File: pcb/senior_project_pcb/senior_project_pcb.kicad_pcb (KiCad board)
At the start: 4 copper layers, 45 x 45 mm, 55 parts, among them IC1 MAX30102, IC2 ZTP-148SRC1, J1 Conn_01x06, J2 USB_B_Micro, Q1 Q_DUAL_NMOS, Q2 Q_DUAL_NMOS_S1G1D2S2G2D1, SW1 SW_Push_Dual, SW2 SW_Push_Dual, U1 stm32wb55ccu6, U2 MIC5504-1.8YM5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

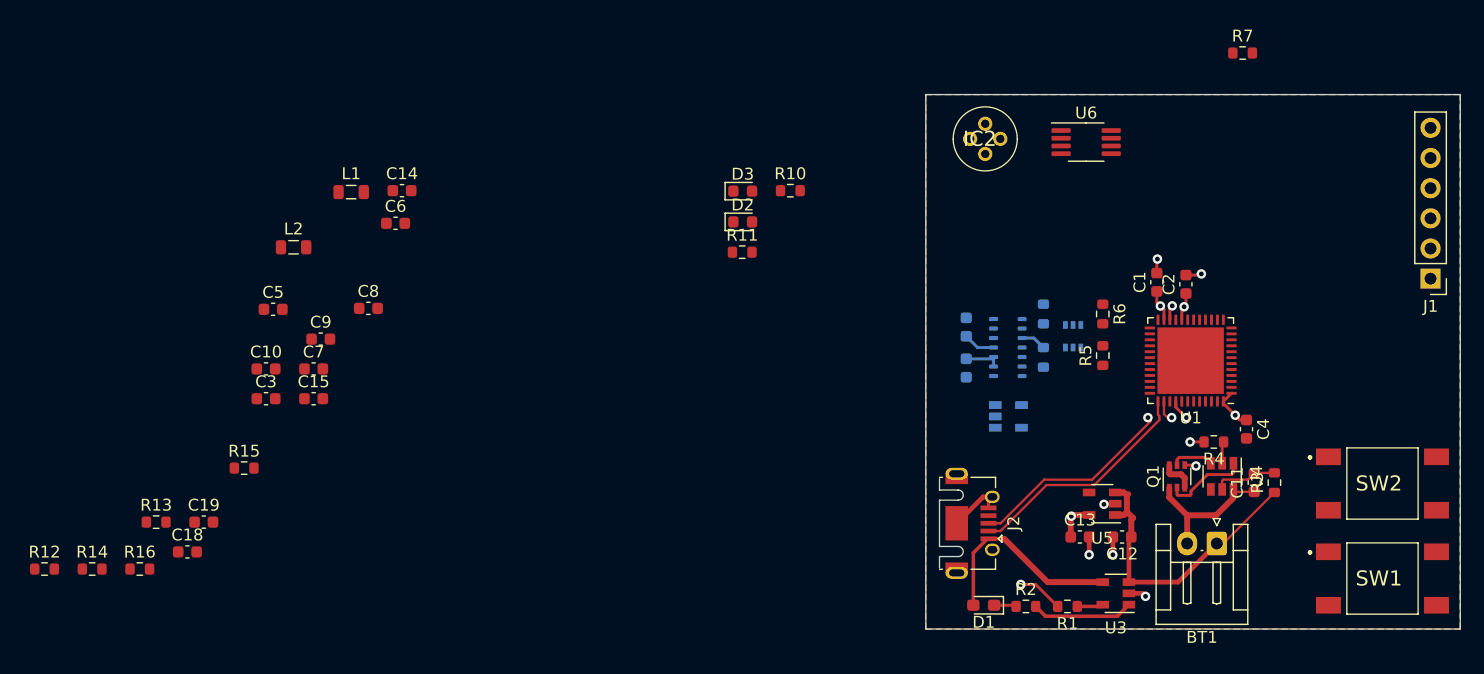
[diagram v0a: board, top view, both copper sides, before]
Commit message: Initial layout mostly done
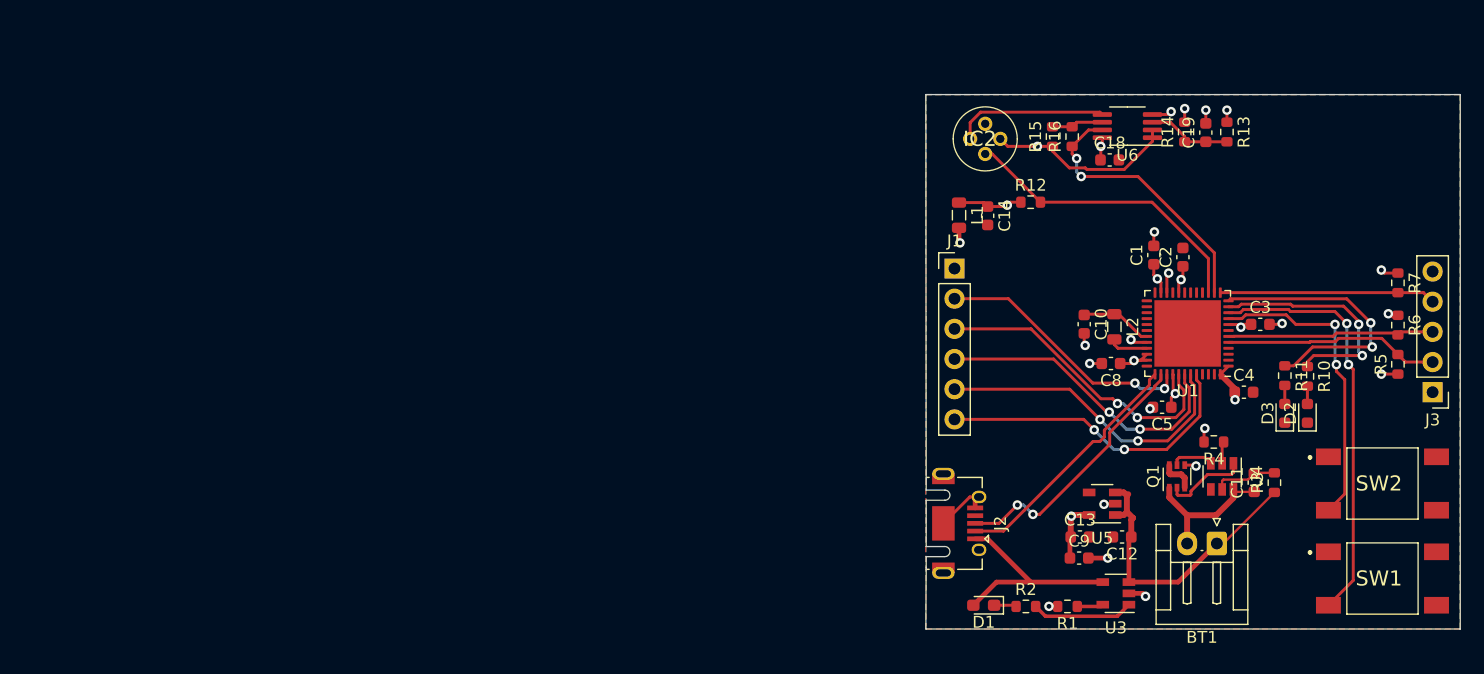
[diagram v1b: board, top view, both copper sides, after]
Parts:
- removed C15: 1u, Capacitor_SMD:C_0603_1608Metric
- removed C16, C17, C6, C7: 100n, Capacitor_SMD:C_0603_1608Metric
- removed IC1: MAX30102, OptoDevice:Maxim_OLGA-14_3.3x5.6mm_P0.8mm
- removed Q2: Q_DUAL_NMOS_S1G1D2S2G2D1, Package_TO_SOT_SMD:SOT-363_SC-70-6
- removed R8, R9: 1k, Resistor_SMD:R_0603_1608Metric
- removed U2: MIC5504-1.8YM5, Package_TO_SOT_SMD:SOT-23-5
- added J3: Conn_01x05, Connector_PinHeader_2.54mm:PinHeader_1x05_P2.54mm_Vertical, F.Cu at (182.7, 75.1)
- C14: value 1u -> 100n
- R5, R6: value 1k -> 2k
- R7: value 10k -> 2k
- moved R14 99.1 mm to (161.8, 53.1), turned to 90 degrees
- moved R13 96.0 mm to (165.4, 53.1), turned to 270 degrees
- moved C19 90.5 mm to (163.6, 53.2), turned to 90 degrees
- moved R12 88.6 mm to (148.8, 59.1)
- moved R16 86.5 mm to (152.3, 53.5), turned to 90 degrees
- moved C18 84.4 mm to (155.5, 55.5)
- moved C3 84.0 mm to (168.2, 69.3)
- moved C5 75.3 mm to (159.9, 76.3), turned to 180 degrees
- moved R15 73.6 mm to (150.7, 53.5), turned to 90 degrees
- moved L2 69.4 mm to (155.9, 69.6), turned to 270 degrees
- moved C10 69.0 mm to (153.3, 69.3), turned to 270 degrees
- moved C9 66.5 mm to (152.9, 89.0)
- moved C8 62.7 mm to (155.6, 72.6), turned to 180 degrees
- moved L1 51.2 mm to (142.8, 60.2), turned to 270 degrees
- moved D2 50.2 mm to (172.1, 76.8), turned to 90 degrees
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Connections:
- C14 pad 1: +3V3 -> +3.3VA
- J1 pad 2: /io/JTAG_TCK -> /io/JTAG_TMS
- J1 pad 3: /io/JTAG_TDI -> /io/JTAG_TCK
- J1 pad 4: /io/JTAG_TDO -> /io/JTAG_TDI
- J1 pad 5: /io/JTAG_TMS -> /io/JTAG_TDO
- R7 pad 2: /Pulse Oximeter/INT -> /INT
- U1 pad 10: /io/LED2 -> /io/BTN1
- U1 pad 11: /io/BTN1 -> /io/LED1
- U1 pad 12: /io/BTN2 -> /io/LED2
- U1 pad 13: Net-(U1-Pad13) -> /INT
- U1 pad 14: Net-(U1-Pad14) -> /thermopile
- U1 pad 15: Net-(U1-Pad15) -> /thermistor
- U1 pad 45: /thermistor -> Net-(U1-Pad45)
- U1 pad 46: /thermopile -> Net-(U1-Pad46)
- U1 pad 9: /io/LED1 -> /io/BTN2
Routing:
- net /io/BTN1: track 0.00 -> 35.4 mm, vias 0 -> 2
- net /io/JTAG_NTRST: track 0.00 -> 26.5 mm, vias 0 -> 2
- net /io/JTAG_TDO: track 0.00 -> 26.4 mm, vias 0 -> 2
- net /io/JTAG_TDI: track 0.00 -> 26.1 mm, vias 0 -> 2
- net /io/BTN2: track 0.00 -> 26.0 mm, vias 0 -> 2
- net /io/JTAG_TCK: track 0.00 -> 25.8 mm, vias 0 -> 2
- net /thermistor: track 0.00 -> 25.3 mm
- net /thermopile: track 0.00 -> 23.2 mm, vias 0 -> 2
- net /io/LED2: track 0.00 -> 23.0 mm, vias 0 -> 2
- net /io/JTAG_TMS: track 0.00 -> 22.1 mm, vias 0 -> 2
- net /io/LED1: track 0.00 -> 19.9 mm, vias 0 -> 2
- net /INT: track 0.00 -> 18.2 mm
- net /SCL: track 0.00 -> 18.2 mm
- net /SDA: track 0.00 -> 17.5 mm
- net /Temperature Sensor/VGND: track 0.00 -> 16.0 mm, vias 0 -> 1
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- added copper zone on In2.Cu, net +3.3VA
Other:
- outline, holes or cut-outs redrawn

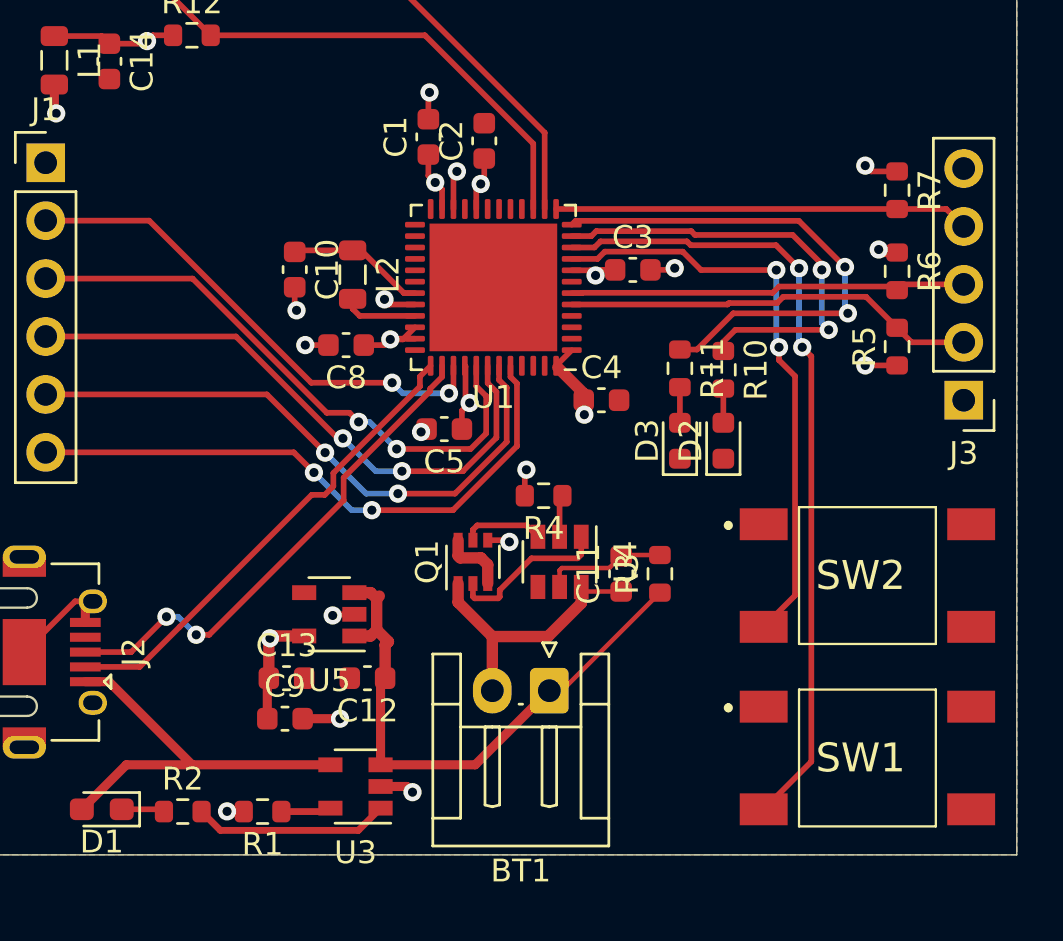
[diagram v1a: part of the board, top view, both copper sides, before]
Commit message: Add ecg sensor
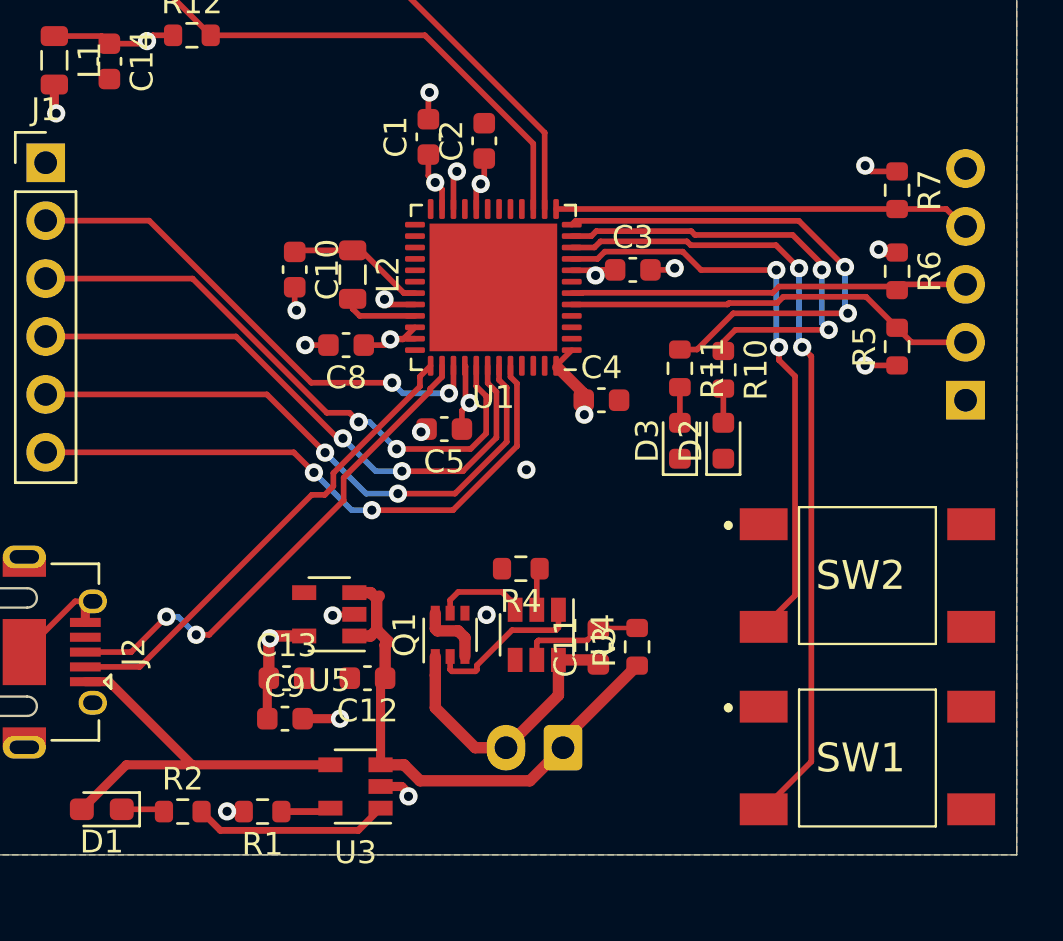
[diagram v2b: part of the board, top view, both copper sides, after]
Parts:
- BT1, J3: moved to B.Cu
- moved C11 3.35 mm to (166.7, 85.9)
- moved R3 3.35 mm to (168.3, 85.9)
- moved R4 3.35 mm to (163.2, 82.5)
- moved Q1 3.35 mm to (160.2, 85.3)
- moved U4 3.35 mm to (163.9, 85.3)
- moved BT1 2.57 mm to (165.1, 90.3)
- moved J3 0.08 mm to (182.8, 75.1), turned to 0 degrees
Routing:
- net GND: track 24.3 -> 22.4 mm
- net +BATT: track 25.4 -> 23.8 mm

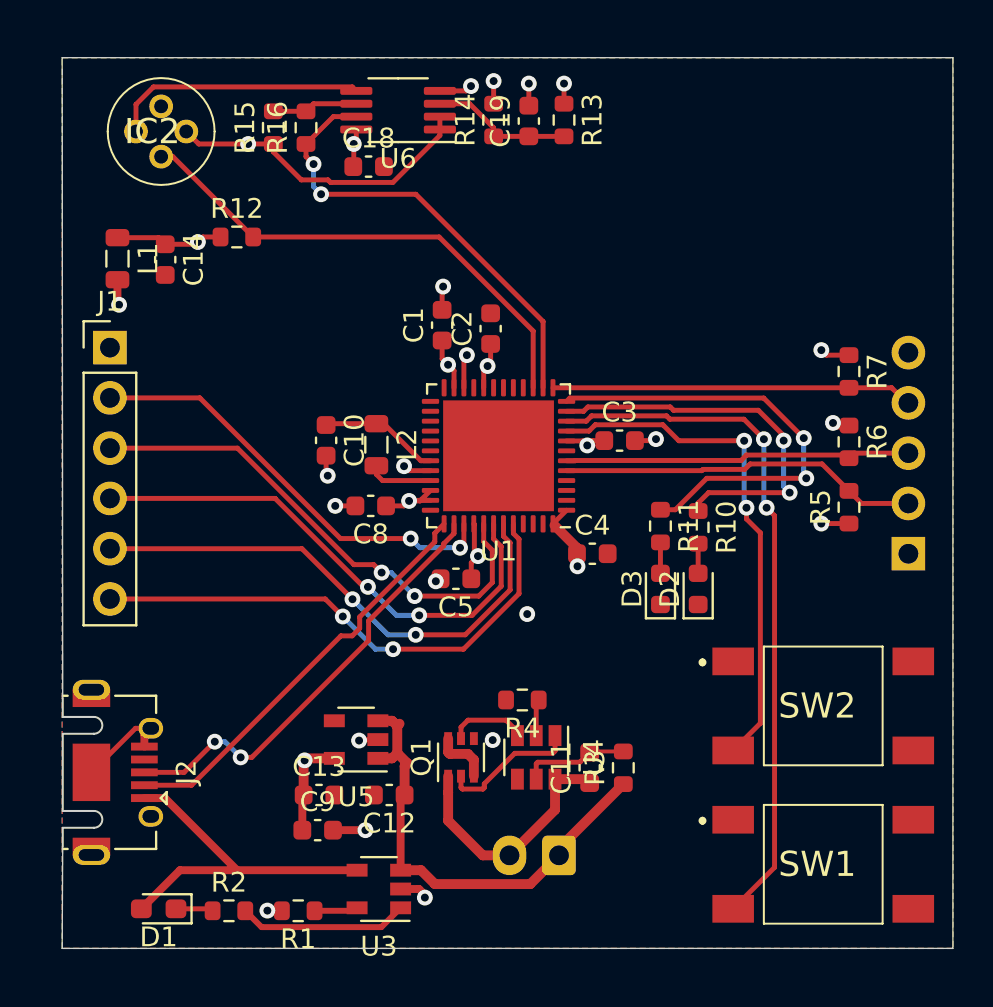
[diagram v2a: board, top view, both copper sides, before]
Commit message: Add RF/Bluetooth to PCB
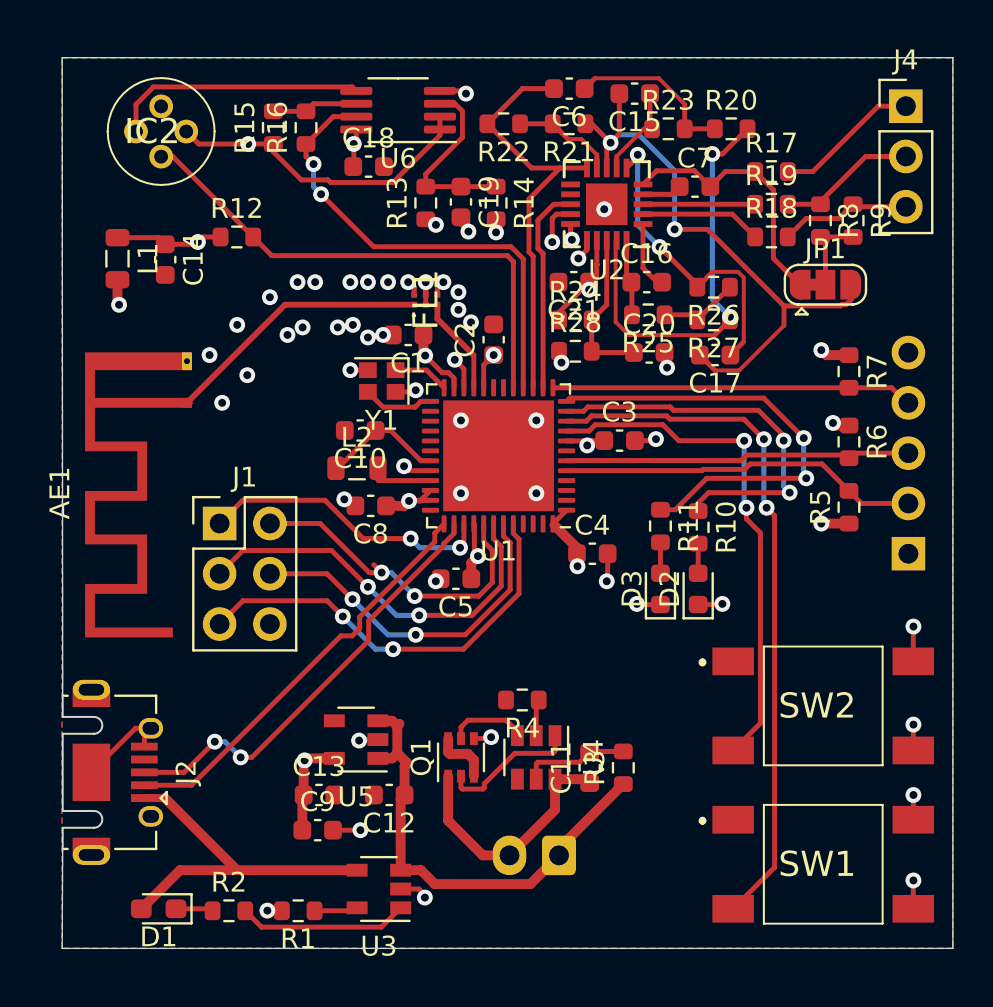
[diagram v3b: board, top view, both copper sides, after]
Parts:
- added AE1: Antenna_Chip, RF_Antenna:Texas_SWRA117D_2.4GHz_Left, F.Cu at (146.3, 67.4)
- added C15: 10n, Capacitor_SMD:C_0603_1608Metric, F.Cu at (168.9, 51.8)
- added C16: .33uF, Capacitor_SMD:C_0603_1608Metric, F.Cu at (169.5, 61.3)
- added C17: .33u, Capacitor_SMD:C_0603_1608Metric, F.Cu at (173.0, 65.0)
- added C20: 100n, Capacitor_SMD:C_0603_1608Metric, F.Cu at (169.7, 64.9)
- added C21: 100n, Capacitor_SMD:C_0603_1608Metric, F.Cu at (165.8, 61.3)
- added C6: 1.5nF, Capacitor_SMD:C_0603_1608Metric, F.Cu at (165.6, 51.6)
- added C7: 1n, Capacitor_SMD:C_0603_1608Metric, F.Cu at (172.0, 56.5)
- added FL1: MLPF-WB55-01E3, kicad_pretty:MLPFWB5501E3, F.Cu at (158.4, 62.2)
- added J4: Conn_01x03, Connector_PinHeader_2.54mm:PinHeader_1x03_P2.54mm_Vertical, F.Cu at (182.6, 52.5)
- added JP1: Jumper_3_Bridged12, Jumper:SolderJumper-3_P1.3mm_Bridged12_RoundedPad1.0x1.5mm, F.Cu at (178.6, 61.5)
- added R17: 360k, Resistor_SMD:R_0603_1608Metric, F.Cu at (175.8, 55.8)
- added R18: 180k, Resistor_SMD:R_0603_1608Metric, F.Cu at (175.8, 59.1)
- added R19: 180k, Resistor_SMD:R_0603_1608Metric, F.Cu at (175.8, 57.4)
- added R20: 1M, Resistor_SMD:R_0603_1608Metric, F.Cu at (173.8, 53.6)
- added R21: 100k, Resistor_SMD:R_0603_1608Metric, F.Cu at (165.6, 53.3)
- added R22: 1M, Resistor_SMD:R_0603_1608Metric, F.Cu at (162.3, 53.3)
- added R23: 1M, Resistor_SMD:R_0603_1608Metric, F.Cu at (170.6, 53.6)
- added R24: 10M, Resistor_SMD:R_0603_1608Metric, F.Cu at (165.9, 63.2)
- added R25: 10M, Resistor_SMD:R_0603_1608Metric, F.Cu at (169.6, 63.0)
- added R26: 1.4M, Resistor_SMD:R_0603_1608Metric, F.Cu at (172.9, 61.6)
- added R27: 10M, Resistor_SMD:R_0603_1608Metric, F.Cu at (172.9, 63.2)
- added R28: 10M, Resistor_SMD:R_0603_1608Metric, F.Cu at (165.9, 64.8)
- added R8: 10M, Resistor_SMD:R_0603_1608Metric, F.Cu at (178.3, 58.2)
- added R9: 10M, Resistor_SMD:R_0603_1608Metric, F.Cu at (180.0, 58.2)
- added U2: AD8232ACPZ-R7, Package_CSP:LFCSP-20-1EP_4x4mm_P0.5mm_EP2.1x2.1mm, F.Cu at (167.5, 57.4)
- added Y1: Crystal_GND24, Crystal:Crystal_SMD_2016-4Pin_2.0x1.6mm, F.Cu at (156.1, 66.3)
- J1: value Conn_01x06 -> Conn_02x03_Odd_Even; footprint Connector_PinHeader_2.54mm:PinHeader_1x06_P2.54mm_Vertical -> Connector_PinHeader_2.54mm:PinHeader_2x03_P2.54mm_Vertical
- moved J1 10.5 mm to (148.0, 73.5)
- moved R13 8.15 mm to (158.4, 57.3), turned to 90 degrees
- moved C19 5.34 mm to (160.1, 57.3), turned to 270 degrees
- moved R14 4.19 mm to (161.9, 57.3), turned to 270 degrees
- moved C10 1.79 mm to (155.1, 68.8), turned to 180 degrees
- moved C1 1.79 mm to (157.5, 64.0), turned to 180 degrees
- moved L2 1.54 mm to (154.9, 70.7), turned to 0 degrees
- moved C2 0.58 mm to (161.8, 64.2)
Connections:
- J1 pad 1: GND -> /io/JTAG_TMS
- J1 pad 2: /io/JTAG_TMS -> /io/JTAG_TCK
- J1 pad 3: /io/JTAG_TCK -> /io/JTAG_TDI
- J1 pad 4: /io/JTAG_TDI -> /io/JTAG_TDO
- J1 pad 5: /io/JTAG_TDO -> /io/JTAG_NTRST
- J1 pad 6: /io/JTAG_NTRST -> GND
- U1 pad 14: /thermopile -> /ECG_SDN
- U1 pad 15: /thermistor -> /ECG_OUT
- U1 pad 16: Net-(U1-Pad16) -> /thermopile
- U1 pad 17: Net-(U1-Pad17) -> /thermistor
- U1 pad 21: Net-(U1-Pad21) -> /rf/Tline
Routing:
- net /ecg/REFOUT: track 0.00 -> 30.7 mm, vias 0 -> 2
- net /ECG_OUT: track 0.00 -> 21.9 mm
- net Net-(R20-Pad2): track 0.00 -> 21.6 mm, vias 0 -> 2
- net GND: track 22.4 -> 39.2 mm, vias 16 -> 49
- net Net-(C17-Pad1): track 0.00 -> 15.8 mm, vias 0 -> 2
- net /rf/TlineANT: track 0.00 -> 13.7 mm
- net /ecg/RLD: track 0.00 -> 13.2 mm
- net /ECG_SDN: track 0.00 -> 10.6 mm
- net /io/JTAG_TCK: track 25.8 -> 16.7 mm
- net /io/JTAG_TDO: track 26.4 -> 17.8 mm
- net Net-(C6-Pad1): track 0.00 -> 8.58 mm
- net Net-(C20-Pad1): track 0.00 -> 8.07 mm
- net /ecg/RL: track 0.00 -> 7.34 mm
- net /io/JTAG_TMS: track 22.1 -> 14.9 mm
- net /ecg/RA: track 0.00 -> 7.04 mm
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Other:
- net class Tline added: clearance 0.127, trace_width 0.29337, via_dia 0.8, via_drill 0.4

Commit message: PCB Update
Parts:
- added G***: luci, kicad_pretty:luci, F.Cu at (169.3, 90.2)
- added L3: 10n, Inductor_SMD:L_0402_1005Metric, F.Cu at (156.6, 71.0)
- added R29: 22, Resistor_SMD:R_0603_1608Metric, F.Cu at (147.9, 86.2)
- added R30: 22, Resistor_SMD:R_0603_1608Metric, F.Cu at (147.9, 84.6)
- BT1: footprint Connector_JST:JST_EH_S2B-EH_1x02_P2.50mm_Horizontal -> Connector_PinHeader_2.54mm:PinHeader_1x02_P2.54mm_Vertical
- C16: value .33uF -> .33u
- D1: footprint LED_SMD:LED_0603_1608Metric_Pad1.05x0.95mm_HandSolder -> LED_SMD:LED_0603_1608Metric
- J2: value USB_B_Micro -> UJ2-MIBH2-4-SMT-TR; footprint Connector_USB:USB_Micro-AB_Molex_47590-0001 -> kicad_pretty:UJ2MIBH24SMTTR
- R12: value 100k -> 100k 1%
- R13, R14: value 10k -> 10k 1%
- R15: value 100 -> 12 1%
- R16: value 49.9k -> 33k 1%
- moved C10 2.44 mm to (153.2, 70.4), turned to 270 degrees
- moved L2 1.73 mm to (155.9, 69.3), turned to 180 degrees
- moved C2 1.17 mm to (161.0, 63.4)
- moved J1 0.85 mm to (148.7, 73.9)
- moved J2 0.35 mm to (141.8, 86.2), turned to 0 degrees
- moved Y1 0.25 mm to (155.9, 66.3)
- turned BT1 to 90 degrees
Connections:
- J2 pad 2: /USB_D- -> Net-(J2-Pad2)
- J2 pad 3: /USB_D+ -> Net-(J2-Pad3)
- U1 pad 10: /io/BTN1 -> Net-(U1-Pad10)
- U1 pad 18: Net-(U1-Pad18) -> /LO+
- U1 pad 19: Net-(U1-Pad19) -> /LO-
- U1 pad 33: Net-(L2-Pad2) -> Net-(L3-Pad1)
- U1 pad 46: Net-(U1-Pad46) -> /io/BTN1
- U1 pad 47: Net-(U1-Pad47) -> /io/BTN2
- U1 pad 49: (no net) -> GND
- U1 pad 9: /io/BTN2 -> Net-(U1-Pad9)
- U2 pad 11: Net-(U2-Pad11) -> /LO-
- U2 pad 12: Net-(U2-Pad12) -> /LO+
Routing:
- net /LO-: track 0.00 -> 14.4 mm, vias 0 -> 2
- net /LO+: track 0.00 -> 12.1 mm, vias 0 -> 2
- net /io/BTN1: track 35.4 -> 23.6 mm, vias 2 -> 0
- net /io/BTN2: track 26.0 -> 15.4 mm, vias 2 -> 0
- net VBUS: track 17.9 -> 24.9 mm
- net /USB_D-: track 21.2 -> 16.0 mm
- net /USB_D+: track 22.4 -> 17.3 mm, vias 2 -> 0
- net Net-(J2-Pad2): track 0.00 -> 3.61 mm
- net Net-(J2-Pad3): track 0.00 -> 3.25 mm
- net (no net): track 2.90 -> 0.00 mm, vias 4 -> 0
- net GND: track 39.2 -> 41.6 mm, vias 49 -> 54
- net Net-(L3-Pad1): track 0.00 -> 1.66 mm
- net /io/JTAG_TCK: track 16.7 -> 15.3 mm
- net Net-(L2-Pad2): track 3.26 -> 2.18 mm
- net /io/JTAG_TMS: track 14.9 -> 14.1 mm
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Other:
- outline, holes or cut-outs redrawn
- board text added: "SPAMM2 PCB V1.0"
